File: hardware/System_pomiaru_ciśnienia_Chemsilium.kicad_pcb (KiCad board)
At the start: 2 copper layers, 50 x 70 mm, 15 parts, among them J1 PRESSURE_SENSOR_1, J1 R_Axial_DIN0204_L3.6mm_D1.6mm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

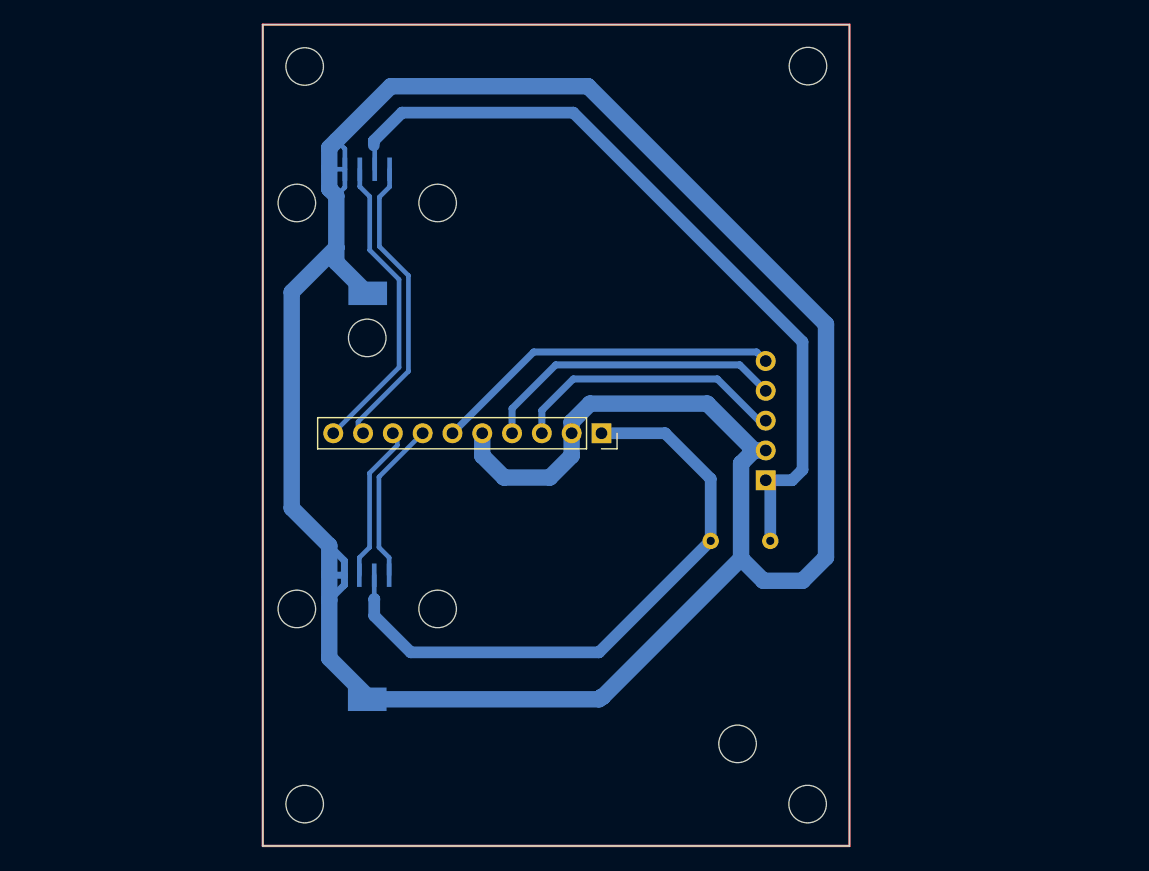
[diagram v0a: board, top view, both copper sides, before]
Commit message: [feat] Initial test design for differential pressure sensor PCB
Initial PCB prototype for differential pressure measurement device.
Identified issues for future iterations:
- UART conflict between STM32 and Arduino Nano.
- Incorrect footprint for MPXM2202 sensor (pitch too small).
- Missing dedicated header for BMP280.
- Insufficient expansion pins (GPIOs for encoder).
- Integrated step-down converter requirement (current version lacks
onboard integration).
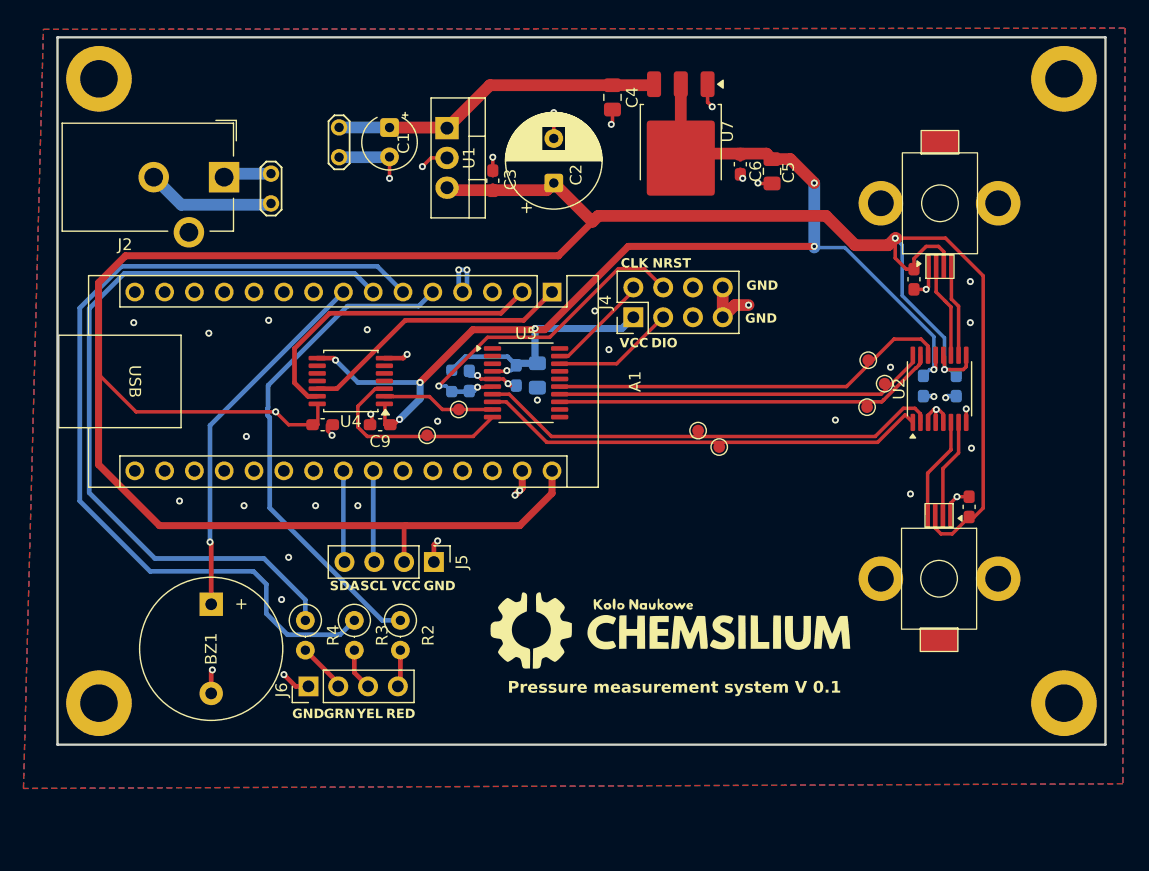
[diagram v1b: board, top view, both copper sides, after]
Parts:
- removed ? (x6): , 
- removed the J1 at (168.9, 112.4)
- removed the J1 at (168.9, 77.8)
- removed the J1 at (203.3, 104.1)
- removed the REF** at (206.5, 63.6)
- removed the REF** at (163.6, 63.7)
- removed the REF** at (188.9, 94.9)
- removed the REF** at (206.4, 126.5)
- removed the REF** at (163.6, 126.5)
- removed the REF** at (202.9, 98.9)
- added A1: Arduino_Nano_v2.x, Module:Arduino_Nano, F.Cu at (184.7, 82.9)
- added BZ1: Buzzer, Buzzer_Beeper:Buzzer_12x9.5RM7.6, F.Cu at (155.6, 109.5)
- added C1: 330n, Capacitor_THT:CP_Radial_Tantal_D4.5mm_P2.50mm, F.Cu at (170.8, 68.9)
- added C10: 100n, Capacitor_SMD:C_0603_1608Metric_Pad1.08x0.95mm_HandSolder, F.Cu at (165.1, 94.2)
- added C11: 100n, Capacitor_SMD:C_0603_1608Metric_Pad1.08x0.95mm_HandSolder, F.Cu at (215.5, 81.8)
- added C12: 100n, Capacitor_SMD:C_0603_1608Metric_Pad1.08x0.95mm_HandSolder, F.Cu at (220.2, 101.2)
- added C13: 100n, Capacitor_SMD:C_0603_1608Metric_Pad1.08x0.95mm_HandSolder, B.Cu at (216.3, 90.9)
- added C14: 100n, Capacitor_SMD:C_0603_1608Metric_Pad1.08x0.95mm_HandSolder, B.Cu at (219.1, 90.9)
- added C15: 100n, Capacitor_SMD:C_0603_1608Metric_Pad1.08x0.95mm_HandSolder, B.Cu at (181.6, 90.0)
- added C16: 10u, Capacitor_SMD:C_0805_2012Metric_Pad1.18x1.45mm_HandSolder, B.Cu at (183.4, 90.0)
- added C17: 100n, Capacitor_SMD:C_0603_1608Metric_Pad1.08x0.95mm_HandSolder, B.Cu at (177.6, 90.5)
- added C2: 100u, Capacitor_THT:CP_Radial_D8.0mm_P3.80mm, F.Cu at (184.8, 73.6)
- added C3: 100n, Capacitor_SMD:C_0603_1608Metric_Pad1.08x0.95mm_HandSolder, F.Cu at (179.6, 73.4)
- added C4: 10u, Capacitor_SMD:C_0805_2012Metric_Pad1.18x1.45mm_HandSolder, F.Cu at (189.8, 66.3)
- added C5: 10u, Capacitor_SMD:C_0805_2012Metric_Pad1.18x1.45mm_HandSolder, F.Cu at (203.4, 72.6)
- added C6: 100n, Capacitor_SMD:C_0603_1608Metric_Pad1.08x0.95mm_HandSolder, F.Cu at (200.7, 72.0)
- added C9: 100n, Capacitor_SMD:C_0603_1608Metric_Pad1.08x0.95mm_HandSolder, F.Cu at (170.0, 94.2)
- added J1: PRESSURE_SENSOR_1, Custom:mpx2202, F.Cu at (217.7, 75.3)
- added J2: Jack-DC, Connector_BarrelJack:BarrelJack_CUI_PJ-102AH_Horizontal, F.Cu at (156.7, 73.1)
- added J3: PRESSURE_SENSOR_2, Custom:mpx2202, F.Cu at (217.7, 107.3)
- added J4: Conn_01x08_Pin, Connector_PinHeader_2.54mm:PinHeader_2x04_P2.54mm_Vertical, F.Cu at (191.6, 85.0)
- added J5: Conn_01x04_Pin, Connector_PinHeader_2.54mm:PinHeader_1x04_P2.54mm_Vertical, F.Cu at (174.6, 105.9)
- added J6: Conn_01x04_Pin, Connector_PinHeader_2.54mm:PinHeader_1x04_P2.54mm_Vertical, F.Cu at (163.9, 116.5)
- added R1: 10k, Resistor_SMD:R_0603_1608Metric_Pad0.98x0.95mm_HandSolder, B.Cu at (176.1, 90.5)
- added R2: 330, Resistor_THT:R_Axial_DIN0207_L6.3mm_D2.5mm_P2.54mm_Vertical, F.Cu at (171.7, 110.9)
- added R3: 330, Resistor_THT:R_Axial_DIN0207_L6.3mm_D2.5mm_P2.54mm_Vertical, F.Cu at (167.8, 110.9)
- added R4: 330, Resistor_THT:R_Axial_DIN0207_L6.3mm_D2.5mm_P2.54mm_Vertical, F.Cu at (163.6, 110.9)
- added REF**: MountingHole_3.2mm_M3_DIN965_Pad, MountingHole:MountingHole_3.2mm_M3_DIN965_Pad, F.Cu at (146.0, 117.9)
- added REF**: MountingHole_2.2mm_M2_DIN965_Pad, MountingHole:MountingHole_2.2mm_M2_DIN965_Pad, F.Cu at (212.7, 75.3)
- added REF**: TestPoint_2Pads_Pitch2.54mm_Drill0.8mm, TestPoint:TestPoint_2Pads_Pitch2.54mm_Drill0.8mm, F.Cu at (160.7, 72.8)
- added REF**: TestPoint_2Pads_Pitch2.54mm_Drill0.8mm, TestPoint:TestPoint_2Pads_Pitch2.54mm_Drill0.8mm, F.Cu at (166.5, 71.4)
- added REF**: TestPoint_Pad_D1.0mm, TestPoint:TestPoint_Pad_D1.0mm, F.Cu at (198.9, 96.1)
- added REF**: TestPoint_Pad_D1.0mm, TestPoint:TestPoint_Pad_D1.0mm, F.Cu at (211.5, 92.7)
- added REF**: TestPoint_Pad_D1.0mm, TestPoint:TestPoint_Pad_D1.0mm, F.Cu at (176.7, 92.9)
- added REF**: MountingHole_2.2mm_M2_DIN965_Pad, MountingHole:MountingHole_2.2mm_M2_DIN965_Pad, F.Cu at (222.7, 75.3)
- added REF**: MountingHole_3.2mm_M3_DIN965_Pad, MountingHole:MountingHole_3.2mm_M3_DIN965_Pad, F.Cu at (146.0, 64.7)
- added REF**: TestPoint_Pad_D1.0mm, TestPoint:TestPoint_Pad_D1.0mm, F.Cu at (213.0, 90.7)
- added REF**: MountingHole_2.2mm_M2_DIN965_Pad, MountingHole:MountingHole_2.2mm_M2_DIN965_Pad, F.Cu at (212.7, 107.3)
- added REF**: MountingHole_2.2mm_M2_DIN965_Pad, MountingHole:MountingHole_2.2mm_M2_DIN965_Pad, F.Cu at (222.7, 107.3)
- added REF**: TestPoint_Pad_D1.0mm, TestPoint:TestPoint_Pad_D1.0mm, F.Cu at (197.1, 94.7)
- added REF**: MountingHole_3.2mm_M3_DIN965_Pad, MountingHole:MountingHole_3.2mm_M3_DIN965_Pad, F.Cu at (228.3, 64.7)
- added REF**: TestPoint_Pad_D1.0mm, TestPoint:TestPoint_Pad_D1.0mm, F.Cu at (211.6, 88.7)
- added REF**: TestPoint_Pad_D1.0mm, TestPoint:TestPoint_Pad_D1.0mm, F.Cu at (174.0, 95.1)
- added REF**: MountingHole_3.2mm_M3_DIN965_Pad, MountingHole:MountingHole_3.2mm_M3_DIN965_Pad, F.Cu at (228.3, 117.9)
- added U1: L7805, Package_TO_SOT_THT:TO-220-3_Vertical, F.Cu at (175.7, 68.9)
- added U2: ADS1220xPW, Package_SO:TSSOP-16_4.4x5mm_P0.65mm, F.Cu at (217.7, 91.1)
- added U4: TXS0104EPW, Package_SO:TSSOP-14_4.4x5mm_P0.65mm, F.Cu at (167.5, 90.5)
- added U5: STM32G030F6Px, Package_SO:TSSOP-20_4.4x6.5mm_P0.65mm, F.Cu at (182.4, 90.6)
- added U7: AMS1117CD-3.3, Package_TO_SOT_SMD:TO-252-3_TabPin2, F.Cu at (195.6, 70.2)
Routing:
- net +5VCC: track 0.00 -> 233.1 mm, vias 0 -> 3
- net GND: track 231.5 -> 68.4 mm, vias 0 -> 49
- net 5V_PRESS_ANALOG: track 122.4 -> 0.00 mm
- net +3VCC: track 0.00 -> 121.0 mm, vias 0 -> 8
- net LED_YELLOW: track 0.00 -> 76.5 mm
- net LED_GREEN: track 0.00 -> 65.8 mm
- net LED_RED: track 0.00 -> 43.0 mm
- net CS_ADC_3V3: track 0.00 -> 39.9 mm
- net SCK_ADC_3V3: track 0.00 -> 38.5 mm
- net DRDY_ADC_3V3: track 0.00 -> 34.1 mm
- net MISO_ADC_3V3: track 0.00 -> 32.8 mm
- net MOSI_ADC_3V3: track 0.00 -> 31.8 mm
- net BUZZER: track 0.00 -> 31.4 mm, vias 0 -> 1
- net (no net): track 29.9 -> 0.00 mm
- net NRST: track 0.00 -> 29.5 mm, vias 0 -> 2
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- added copper zone on B.Cu, net GND
- added copper zone on F.Cu, net GND
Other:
- board size 50 x 70 mm -> 89.3 x 60.3 mm
- board text added: "CLK"
- board text added: "DIO"
- board text added: "GRN"
- board text added: "NRST"
- board text added: "Pressure measurement system V 0.1"
- board text added: "RED"
- board text added: "YEL"
- board text removed: "A0"
- board text removed: "A1"
- board text removed: "A2"
- board text removed: "A3"
- board text removed: "ADDR"
- board text removed: "ALERT"
